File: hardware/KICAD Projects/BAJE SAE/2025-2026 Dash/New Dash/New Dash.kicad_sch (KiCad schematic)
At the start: 19 parts, among them J1 CAN to outer connector, J1-1 Conn_01x05, J1-2 Conn_01x05, J10 Servo 1 (RPM), J11-1 Conn_01x05, J11-2 Conn_01x05, J12 Conn_01x02, J2 Servo 2 (Speed), J4 Button 1, J5 14 Segment (1), J6 14 Segment (2), J7 14 Segment (3), J8 14 Segment (4), J9 Button 2, J999 Conn_01x06, U1 XIAO-ESP32-S3-SMD

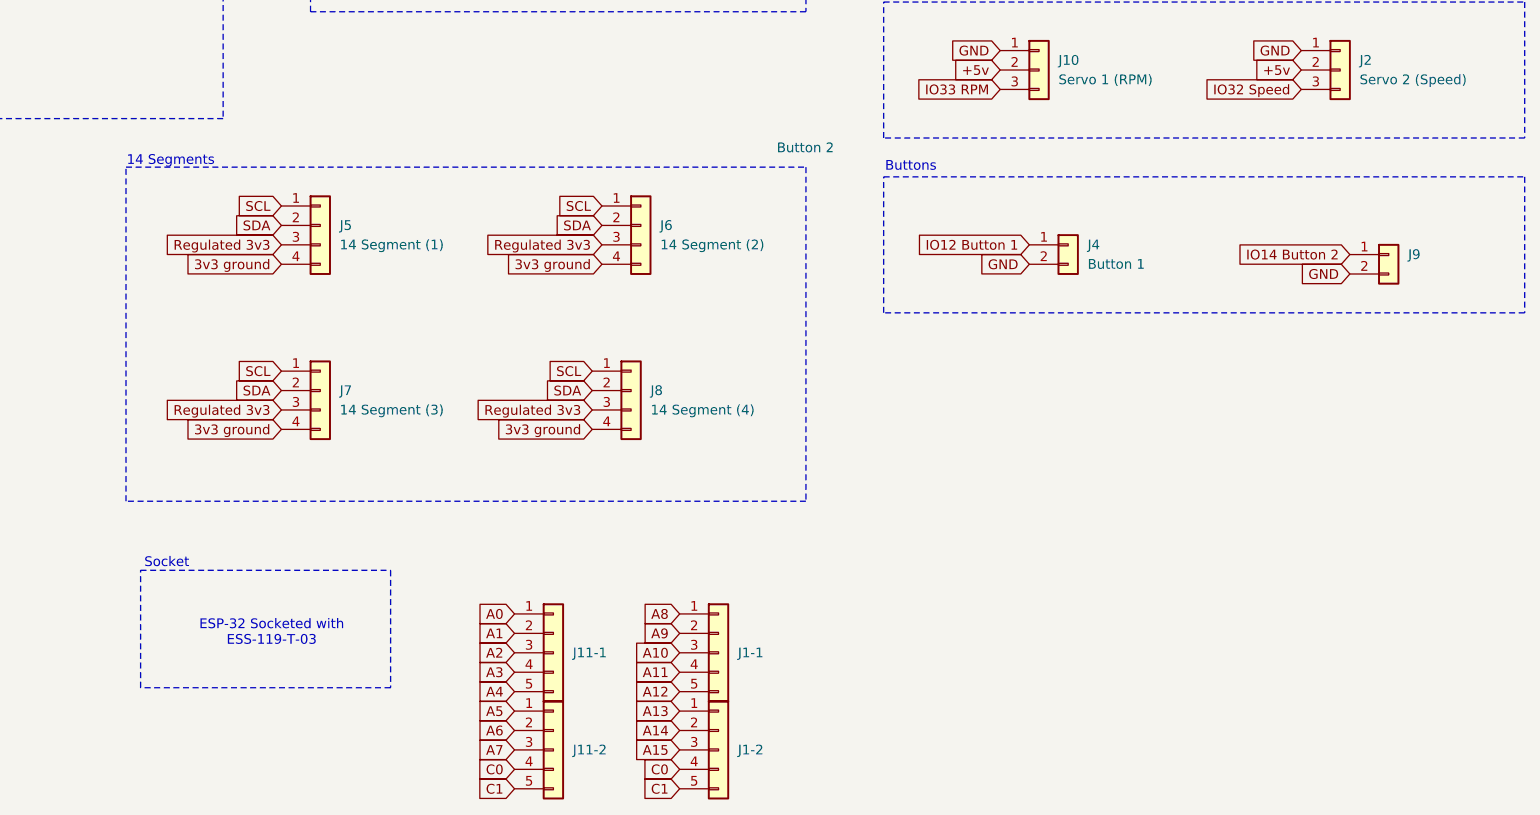
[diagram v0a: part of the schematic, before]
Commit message: Updating Final Dash setup
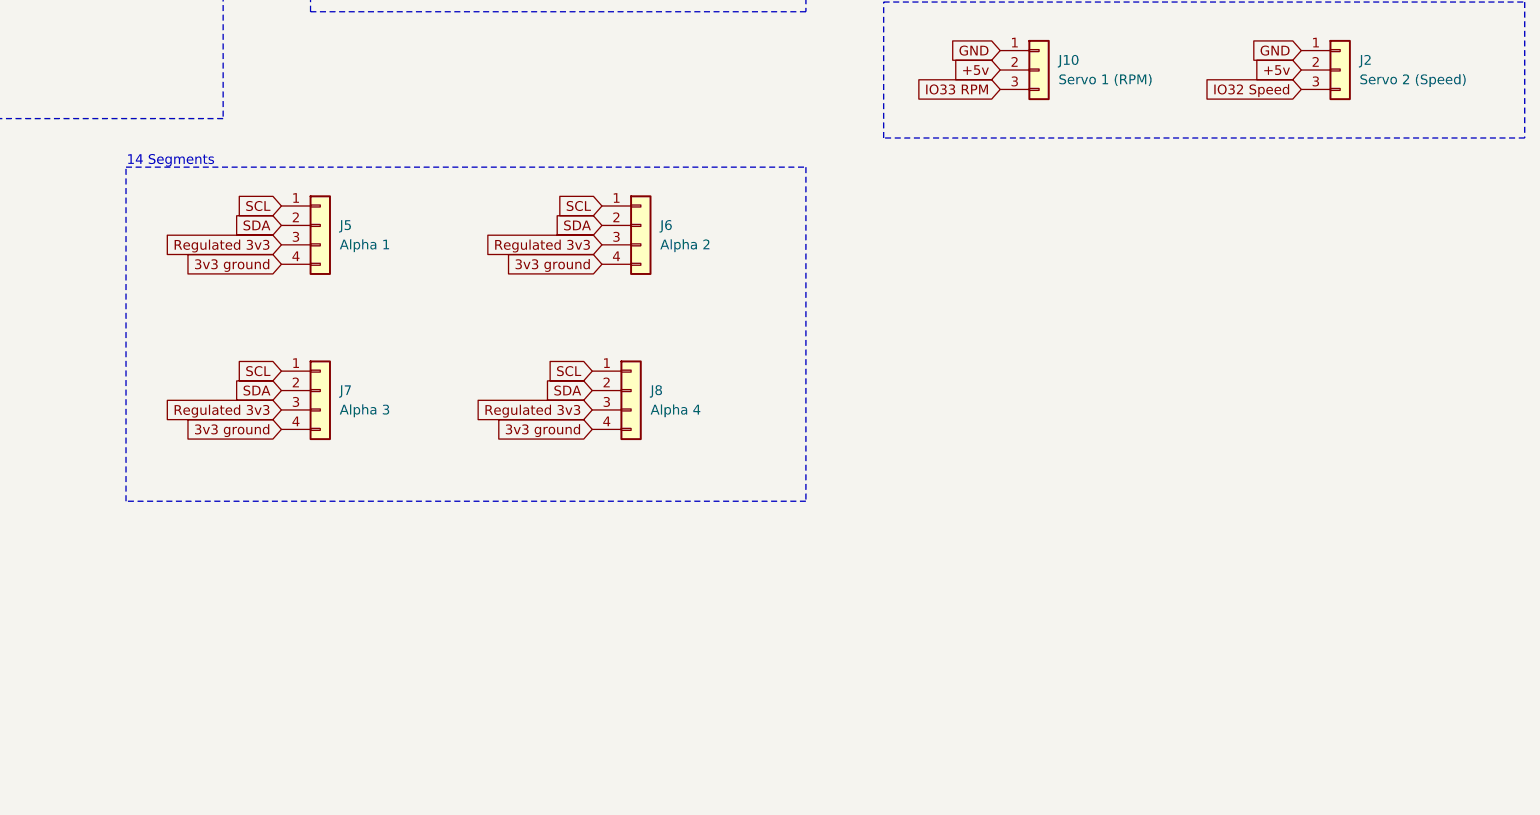
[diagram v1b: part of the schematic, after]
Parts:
- removed J1-1, J1-2, J11-1, J11-2: Conn_01x05, Connector_PinHeader_2.54mm:PinHeader_1x05_P2.54mm_Vertical, symbol Connector_Generic:Conn_01x05
- removed J4: Button 1, Connector_PinHeader_2.54mm:PinHeader_1x02_P2.54mm_Vertical, symbol Connector_Generic:Conn_01x02
- removed J9: Button 2, Connector_PinHeader_2.54mm:PinHeader_1x02_P2.54mm_Vertical, symbol Connector_Generic:Conn_01x02
- J5: value 14 Segment (1) -> Alpha 1
- J6: value 14 Segment (2) -> Alpha 2
- J7: value 14 Segment (3) -> Alpha 3
- J8: value 14 Segment (4) -> Alpha 4
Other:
- note removed: "Buttons"
- note removed: "ESP-32 Socketed with ESS-119-T-03"
- note removed: "Socket"
